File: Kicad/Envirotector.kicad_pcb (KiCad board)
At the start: 2 copper layers, 75 x 77.7 mm, 11 parts, among them J1 OLED Display, SW1 RotaryEncoder_Switch, U1 XIAO-RP2040-DIP, U2 DHT11

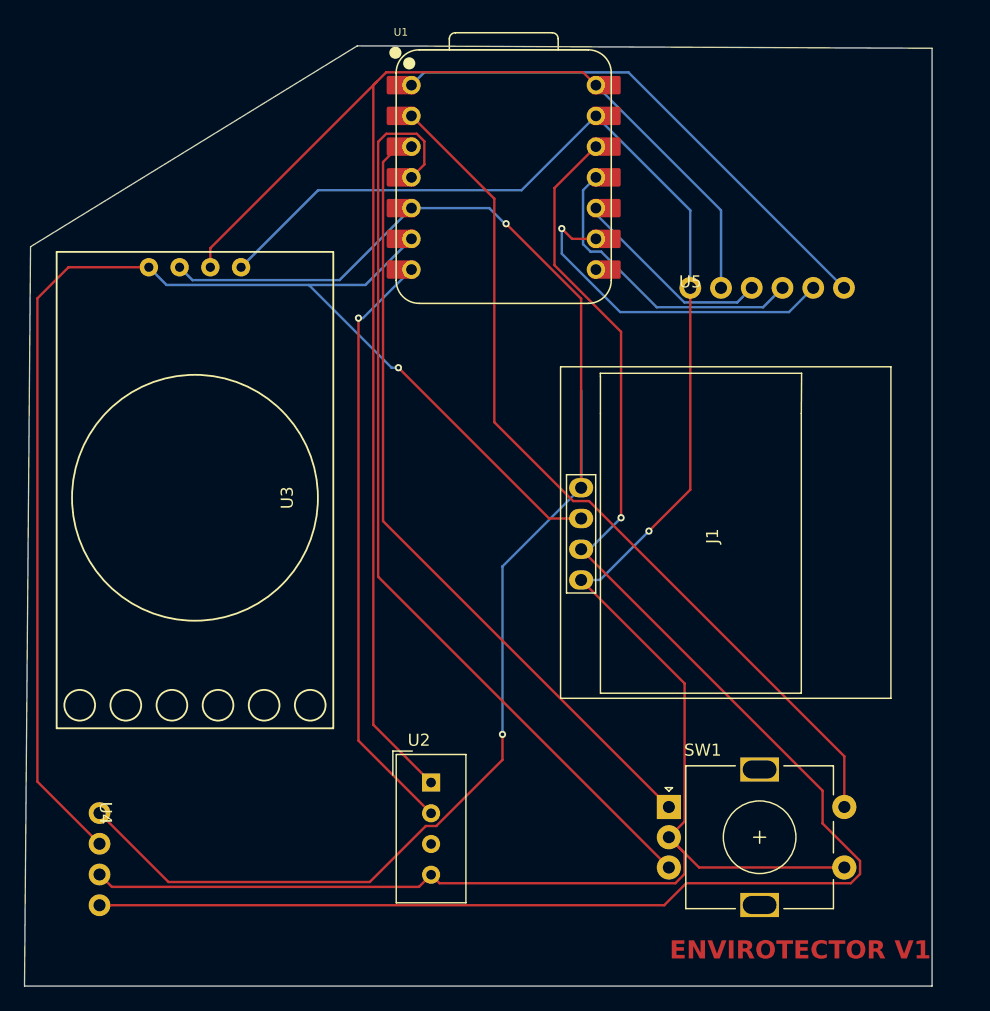
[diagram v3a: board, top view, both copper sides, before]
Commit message: rerouted pcb and updated silkscreen
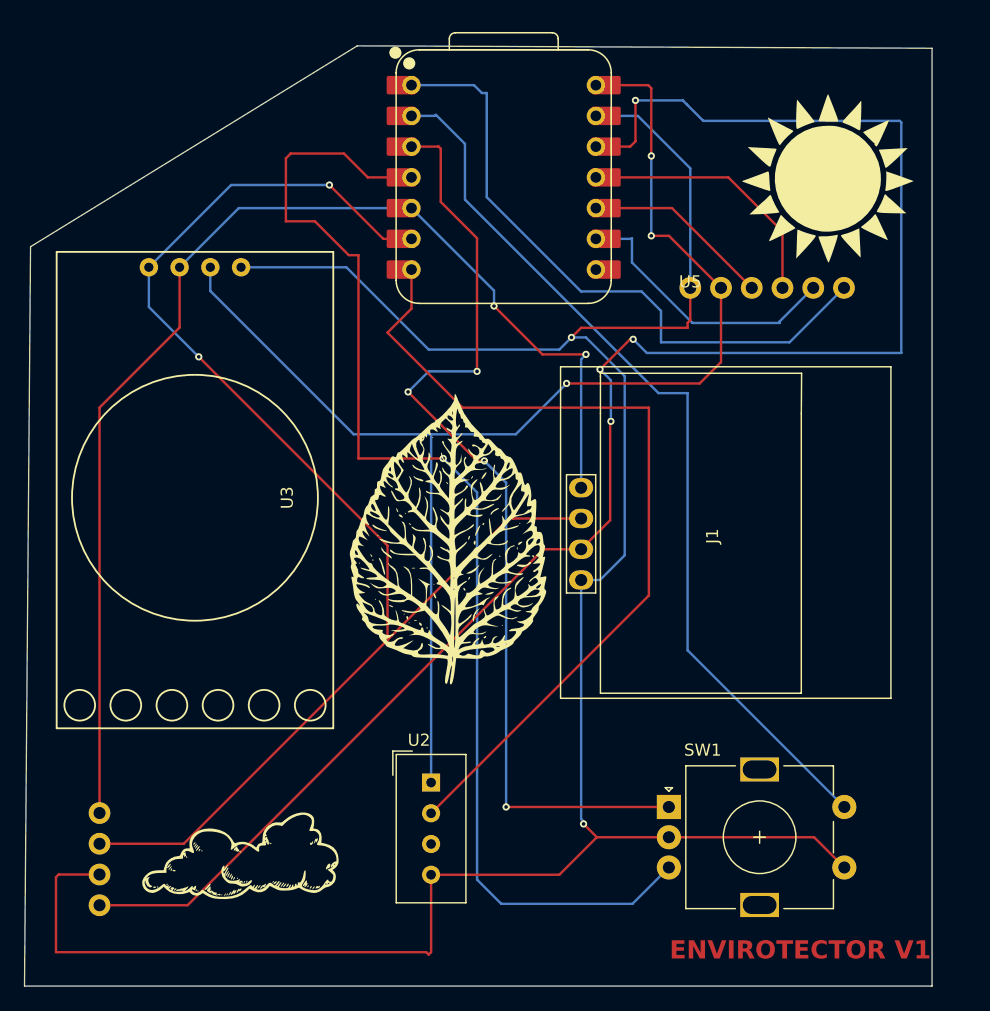
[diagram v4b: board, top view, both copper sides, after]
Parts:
- removed the G*** at (90.3, 121.3)
- removed the G*** at (133.3, 72.8)
- removed the G*** at (106.6, 91.1)
- added G***: LOGO, LOGO, F.Cu at (136.3, 68.1)
- added G***: LOGO, LOGO, F.Cu at (104.6, 97.9)
- added G***: LOGO, LOGO, F.Cu at (87.8, 123.7)
- added G***: LOGO, LOGO, B.Cu at (88.4, 93.8)
- moved G*** 14.6 mm to (131.4, 103.5)
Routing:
- net Net-(J1-Pin_1): track 127.9 -> 100.4 mm
- net Net-(U1-GPIO29/ADC3/A3): track 77.7 -> 101.4 mm, vias 0 -> 1
- net Net-(U1-GPIO0/TX): track 49.5 -> 71.2 mm, vias 1 -> 0
- net GND: track 175.0 -> 194.0 mm, vias 1 -> 2
- net Net-(U1-GPIO28/ADC2/A2): track 66.0 -> 80.2 mm, vias 0 -> 4
- net +5V: track 120.9 -> 110.9 mm, vias 0 -> 3
- net Net-(U1-GPIO26/ADC0/A0): track 43.6 -> 53.0 mm
- net Net-(U1-GPIO2/SCK): track 28.9 -> 23.3 mm, vias 1 -> 0
- net +3.3V: track 139.1 -> 143.3 mm, vias 1 -> 4
- net Net-(J1-Pin_2): track 112.5 -> 116.4 mm, vias 1 -> 2
- net Net-(U1-GPIO3/MOSI): track 25.3 -> 21.9 mm
- net Net-(U1-GPIO27/ADC1/A1): track 72.7 -> 74.6 mm
- net Net-(U1-GPIO4/MISO): track 16.9 -> 15.6 mm

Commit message: updated microsd card reader
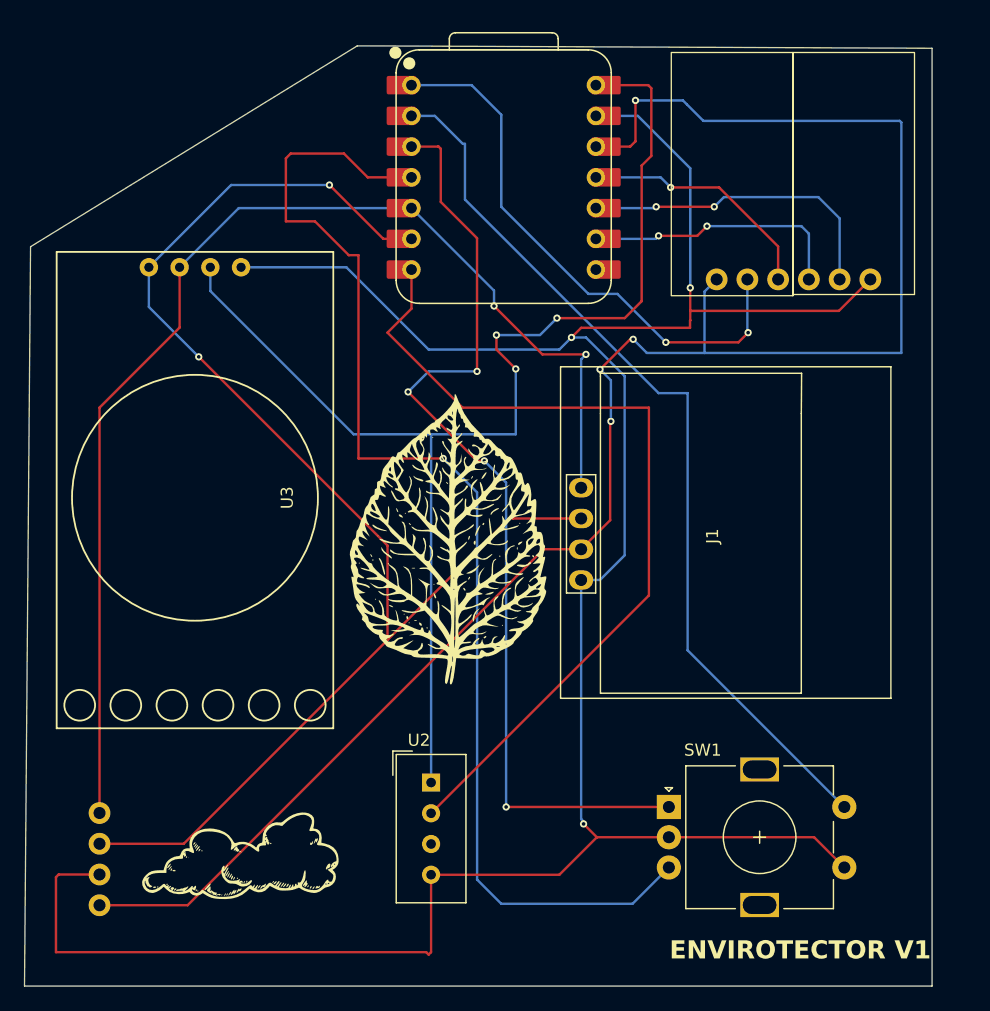
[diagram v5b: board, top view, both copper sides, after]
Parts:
- G***: moved to B.Cu
- moved U5 14.9 mm to (139.9, 76.6), turned to 180 degrees
- turned G*** to 180 degrees
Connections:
- U5 pad 2: +5V -> +3.3V
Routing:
- net GND: track 194.0 -> 210.1 mm, vias 2 -> 3
- net Net-(U1-GPIO4/MISO): track 15.6 -> 26.3 mm, vias 0 -> 2
- net Net-(U1-GPIO26/ADC0/A0): track 53.0 -> 45.8 mm, vias 0 -> 2
- net +3.3V: track 143.3 -> 149.8 mm
- net +5V: track 110.9 -> 105.5 mm
- net Net-(U1-GPIO3/MOSI): track 21.9 -> 20.1 mm, vias 0 -> 1
- net Net-(U1-GPIO2/SCK): track 23.3 -> 22.1 mm, vias 0 -> 2
